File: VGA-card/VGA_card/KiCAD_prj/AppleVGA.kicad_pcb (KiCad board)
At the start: 2 copper layers, 112.4 x 66.7 mm, 35 parts, among them J1 AppleIIBus, J2 VGA, Q1 DMG2305UX-7, SW1 Reset, U1 74LVC245, U2 74LVC245, U3 74LVC245, U4 74LVC245, U6 Pico

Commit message: VGA card KiCAD project updated
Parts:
- removed J2: VGA, Connector_IDC:IDC-Header_2x04_P2.54mm_Vertical
- added J3: DE15_HD_Female, Connector_Dsub:DSUB-15-HD_Female_Horizontal_P2.29x1.98mm_EdgePinOffset8.35mm_Housed_MountingHolesOffset10.89mm, F.Cu at (200.8, 36.1)
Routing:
- net VGA_HSYNC: track 44.7 -> 0.00 mm
- net VGA_VSYNC: track 31.7 -> 0.00 mm
- net VGA_B: track 19.4 -> 6.35 mm
- net VGA_R: track 17.3 -> 5.08 mm
- net VGA_G: track 17.0 -> 5.08 mm
- net GND: vias 16 -> 13

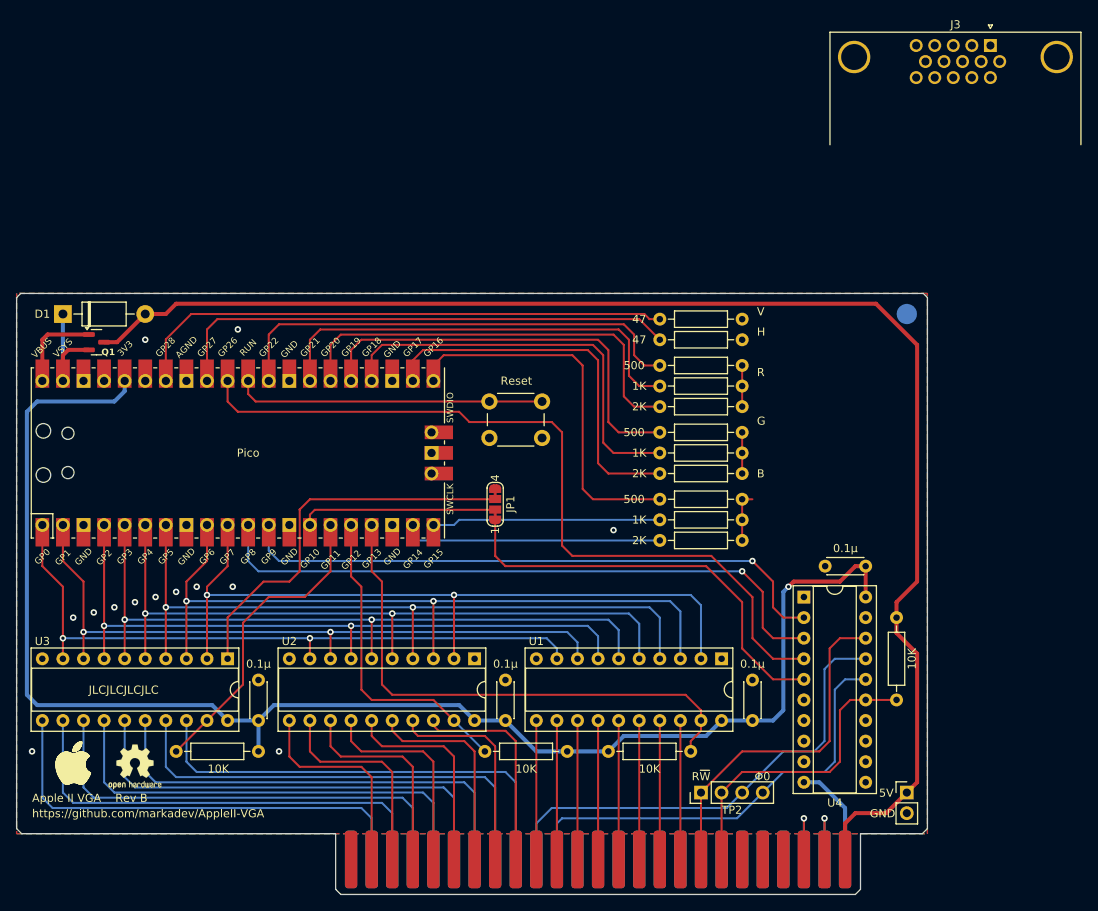
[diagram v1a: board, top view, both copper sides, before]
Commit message: VGA card KiCAD updated
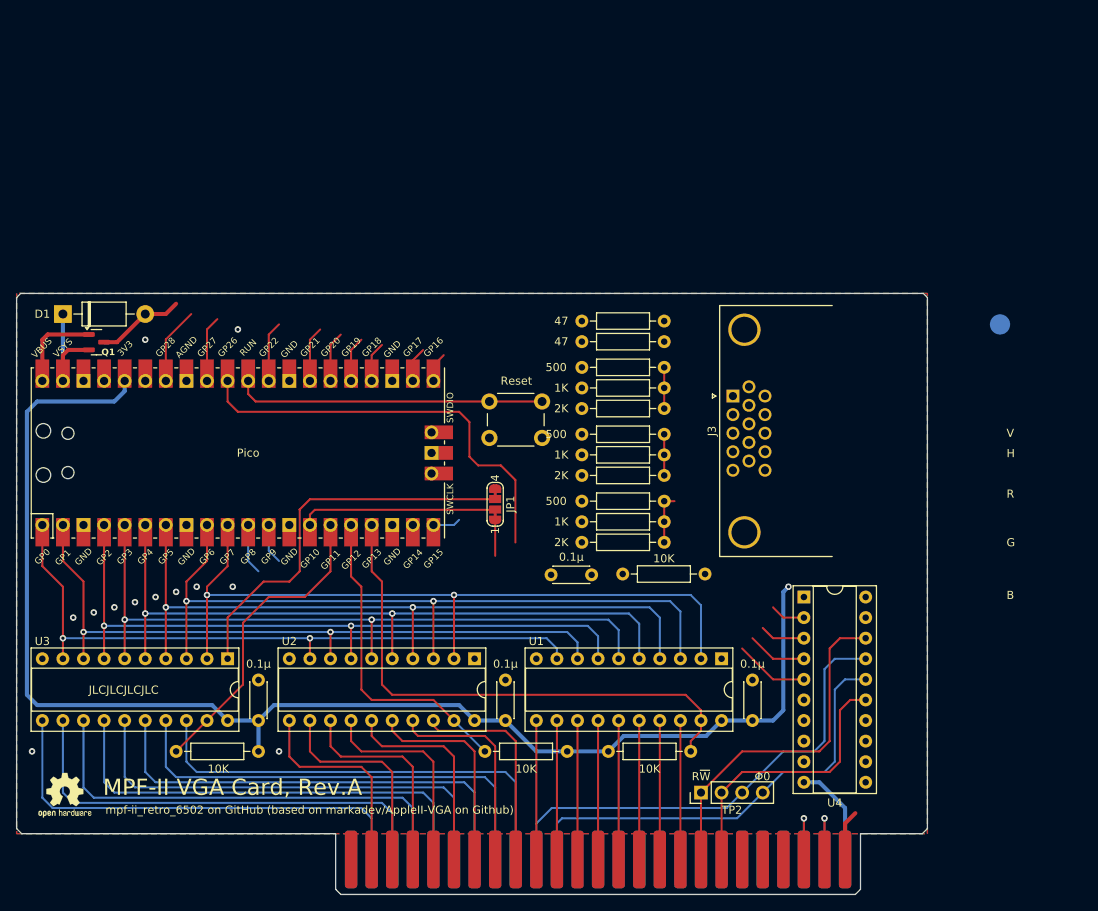
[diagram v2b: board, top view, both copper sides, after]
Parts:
- removed LOGO1: AppleLogo_5mm, AppleVGA:AppleLogo_5mm
- removed TP1: PowerTestPoints, Connector_PinHeader_2.54mm:PinHeader_1x02_P2.54mm_Vertical
- moved J3 53.7 mm to (169.0, 79.3), turned to 90 degrees
- moved R15 34.2 mm to (155.4, 101.3), turned to 0 degrees
- moved C4 33.8 mm to (151.6, 101.4)
- moved REF** 11.6 mm to (202.0, 70.5)
- moved R10 9.62 mm to (150.4, 92.3)
- moved R11 9.62 mm to (150.4, 94.8)
- moved R12 9.62 mm to (150.4, 97.4)
- moved R13 9.62 mm to (150.4, 70.1)
- moved R14 9.62 mm to (150.4, 72.6)
- moved R4 9.62 mm to (150.4, 75.8)
- moved R5 9.62 mm to (150.4, 78.3)
- moved R6 9.62 mm to (150.4, 80.9)
- moved R7 9.62 mm to (150.4, 84.1)
- moved R8 9.62 mm to (150.4, 86.6)
- moved R9 9.62 mm to (150.4, 89.1)
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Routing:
- net +5V: track 175.9 -> 17.1 mm
- net Net-(U4-A1): track 79.6 -> 11.8 mm, vias 1 -> 0
- net Net-(U4-A0): track 74.5 -> 9.31 mm, vias 1 -> 0
- net Net-(U6-GPIO28_ADC2): track 67.6 -> 9.55 mm
- net Net-(U6-GPIO27_ADC1): track 63.8 -> 8.15 mm
- net Net-(U6-GPIO22): track 58.1 -> 7.51 mm
- net Net-(U6-GPIO21): track 54.3 -> 6.88 mm
- net Net-(U6-GPIO19): track 52.4 -> 5.61 mm
- net Net-(U6-GPIO20): track 53.0 -> 6.24 mm
- net Net-(U6-GPIO18): track 51.1 -> 4.97 mm
- net Net-(U6-GPIO16): track 44.8 -> 1.80 mm
- net Net-(U6-GPIO17): track 47.3 -> 4.34 mm
- net Net-(JP1-Pin_1): track 52.1 -> 13.6 mm
- net PHI0_3.3: track 98.0 -> 59.7 mm
- net Net-(U6-GPIO14): track 32.0 -> 2.17 mm
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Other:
- board text added: "MPF-II VGA Card, Rev.A"
- board text added: "mpf-ii_retro_6502 on GitHub (based on markadev/AppleII-VGA on Github)"
- board text removed: "5V"
- board text removed: "Apple II VGA Rev B"
- board text removed: "GND"
- board text removed: "https://github.com/markadev/AppleII-VGA"
